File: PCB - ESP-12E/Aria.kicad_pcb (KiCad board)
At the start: 4 copper layers, 80 x 27 mm, 90 parts, among them J1 B2B-PH-K-S(LF)(SN), J2 B3B-PH-K-S(LF)(SN), J3 20021121-00010C4LF, J4 0475890001-MicroUSBPort, P1 CONN_01X18, P2 CONN_01X18, Q1 DMG2307L-7, Q2 DMG2307L-7, SW1 B3U-1000P, SW2 B3U-1000P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

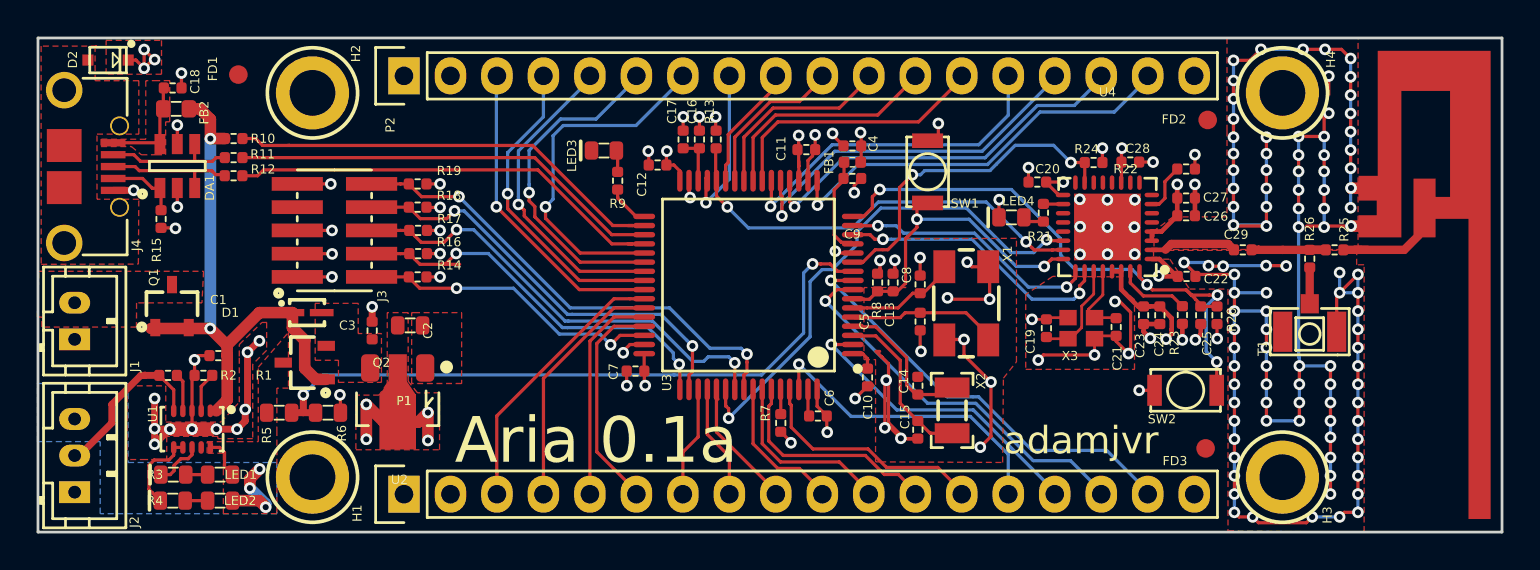
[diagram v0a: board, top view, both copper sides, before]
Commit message: ESP Footprint Error and RF improvement
ESP8285 footprint was wrong, made when I was still learning kiCAD.
Footprint change and entire topology reconstructed and rerouted. Added
ground pours and heavy via stitching to improve RF performance. Also
started an ESP-12E module based variant. Both will be fabbed at the same
time.
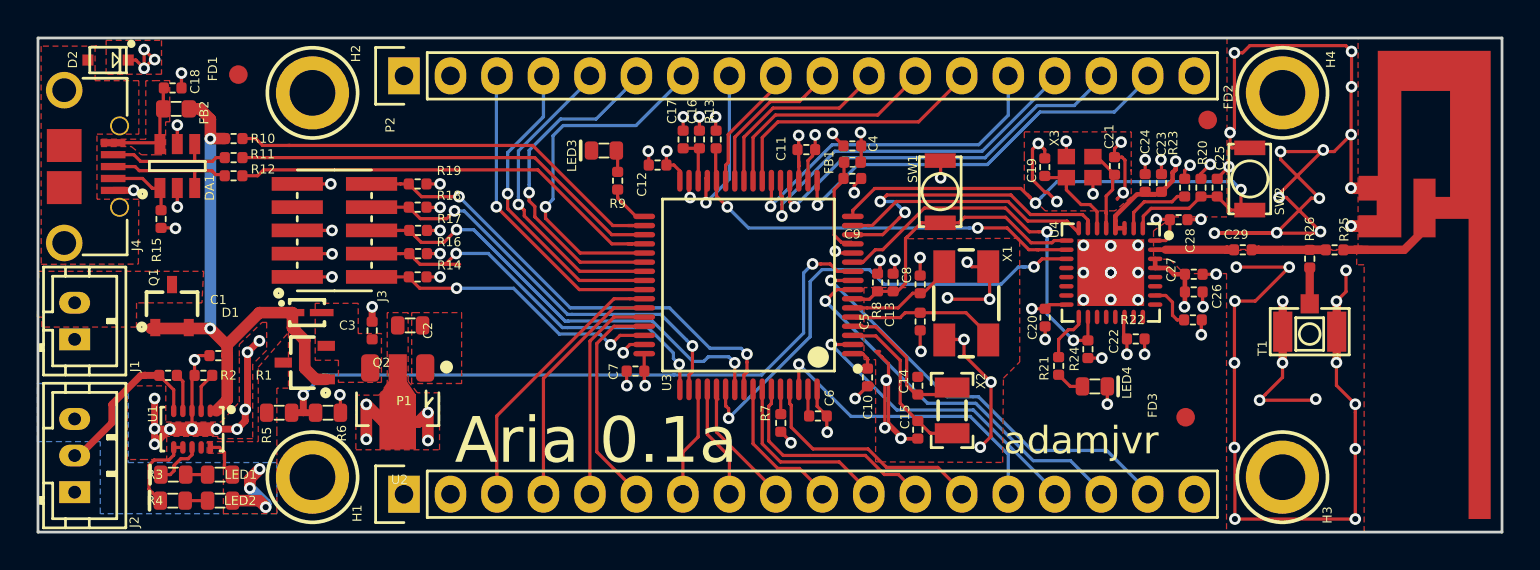
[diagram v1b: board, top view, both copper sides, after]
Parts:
- moved SW2 12.1 mm to (212.1, 79.3), turned to 270 degrees
- moved LED4 10.3 mm to (203.6, 90.6), turned to 0 degrees
- moved R24 10.2 mm to (203.2, 88.6), turned to 90 degrees
- moved C19 8.80 mm to (200.9, 78.6)
- moved X3 8.80 mm to (202.8, 78.6)
- moved C21 8.80 mm to (204.7, 78.6), turned to 90 degrees
- moved R21 8.41 mm to (201.6, 89.5), turned to 90 degrees
- moved R22 8.25 mm to (209.0, 87.0)
- moved C20 7.42 mm to (200.9, 86.9), turned to 270 degrees
- moved C23 7.29 mm to (207.3, 79.5), turned to 90 degrees
- moved C24 7.27 mm to (206.4, 79.5), turned to 90 degrees
- moved C25 7.03 mm to (210.3, 79.8), turned to 90 degrees
- moved R20 7.03 mm to (209.4, 79.8), turned to 90 degrees
- moved R23 6.96 mm to (208.5, 79.8), turned to 270 degrees
- moved C22 4.40 mm to (205.9, 88.0)
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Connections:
- R21 pad 1: Net-(R21-Pad1) -> Net-(LED4-Pad1)
- R21 pad 2: Net-(LED4-Pad1) -> Net-(R21-Pad2)
- U4 pad 16: Net-(U4-Pad16) -> Net-(R21-Pad2)
- U4 pad 18: Net-(R21-Pad1) -> Net-(U4-Pad18)
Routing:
- net GND: track 241.3 -> 218.1 mm, vias 172 -> 105
- net /MCU_STM32F446RET6/ESP_URX: track 15.3 -> 18.1 mm
- net Net-(R21-Pad2): track 0.00 -> 2.81 mm
- net /MCU_STM32F446RET6/ESP_PGM_MODE: track 18.4 -> 21.0 mm
- net /MCU_STM32F446RET6/ESPTOST_BOOT0: track 28.2 -> 26.2 mm
- net /MCU_STM32F446RET6/ESP_ST_RST: track 17.1 -> 15.5 mm, vias 2 -> 0
- net Net-(R21-Pad1): track 1.08 -> 0.00 mm
- net /MCU_STM32F446RET6/STM_ESP_RST: track 32.6 -> 31.7 mm, vias 4 -> 2
- net /MCU_STM32F446RET6/ESPTOST_BOOT1: track 23.7 -> 22.8 mm
- net /MCU_STM32F446RET6/ESP_UTX: track 14.1 -> 13.7 mm, vias 2 -> 0
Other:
- net class Default: clearance 0.1524 -> 0.1778
- rule trace_clearance: 0.1524 -> 0.1778
- rule trace_min: 0.1524 -> 0.1778

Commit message: DRC Cleared and Pictures
DRC cleared of errors for both Aria board designs. New pictures have
been added. Readme has also been updated.
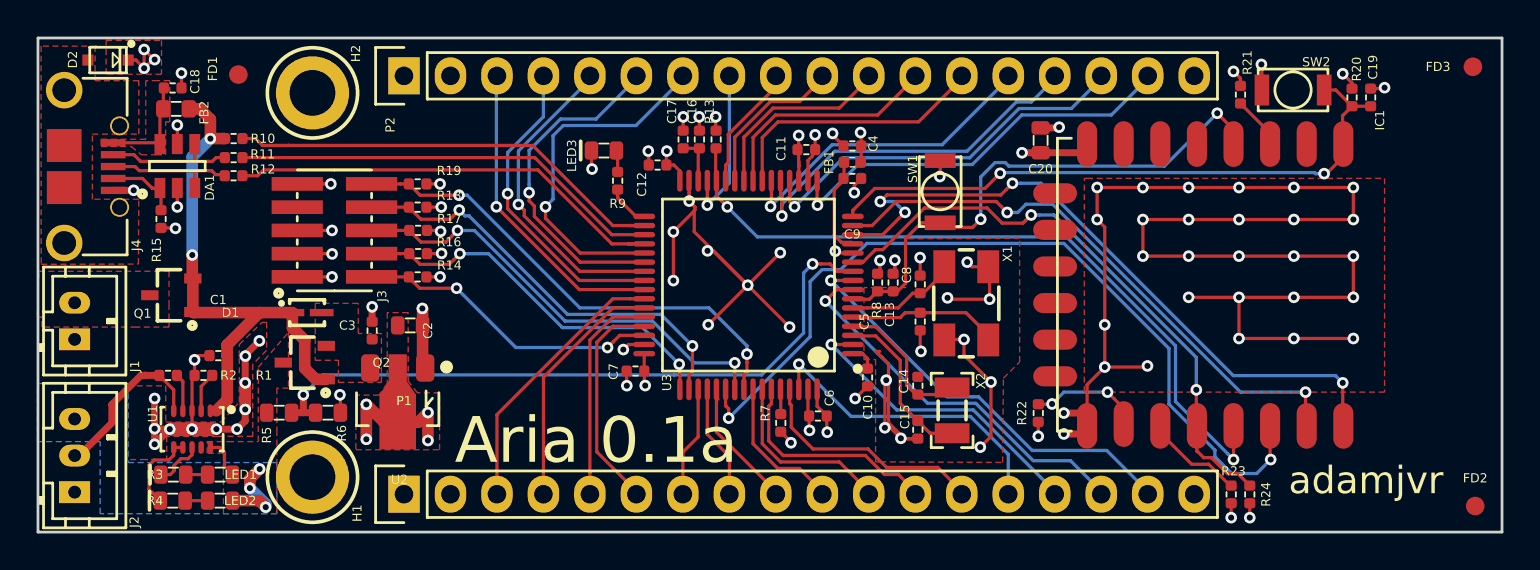
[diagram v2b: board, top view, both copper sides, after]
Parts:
- removed ANT1: Inverted_F_PCB_Antenna, PCB_Footprints:PCB_IF_ANT_2.4G
- removed C21: CL05C090CB5NNNC, PCB_Footprints:C0402
- removed C22, C23, C24, C25, C26, C27, C28: CL05B104JP5NNNC, PCB_Footprints:C0402
- removed C29: 600L5R6BT200T, PCB_Footprints:C0402
- removed H3, H4: M2.5_Hole, PCB_Footprints:M2.5_HOLE
- removed LED4: LTST-C193TBKT-5A, PCB_Footprints:LED0603
- removed R25, R26: ERJ-2GE0R00X, PCB_Footprints:R0402
- removed T1: 1909763-1, PCB_Footprints:1909763-1
- removed U4: ESP8285, PCB_Footprints:ESP8285
- removed X3: FA-128_26.0000MF10Z-AC3, PCB_Footprints:FA-128_26.0000MF10Z-AC3
- added IC1: ESP_12E, PCB_Footprints:ESP-12E, F.Cu at (217.2, 78.1)
- C19: value CL05C090CB5NNNC -> CL05B104JP5NNNC
- C20: value CL05B104JP5NNNC -> CL10A106KQ8NNNC; footprint PCB_Footprints:C0402 -> PCB_Footprints:C0603
- R21: value RC1005F102CS -> RC1005F103CS
- R22, R23: value RC1005F123CS -> RC1005F103CS
- moved FD2 25.7 mm to (224.4, 97.2)
- moved FD3 24.8 mm to (224.3, 73.2)
- moved C19 18.2 mm to (218.7, 74.8)
- moved R21 17.8 mm to (211.6, 74.7), turned to 270 degrees
- moved R23 17.0 mm to (211.1, 96.5), turned to 90 degrees
- moved R24 11.9 mm to (212.1, 96.5)
- moved R22 9.87 mm to (200.5, 92.1), turned to 270 degrees
- moved C20 9.69 mm to (200.7, 77.2), turned to 90 degrees
- moved R20 9.61 mm to (217.7, 74.8), turned to 270 degrees
- moved SW2 5.41 mm to (214.5, 74.4), turned to 0 degrees
- moved Q1 0.59 mm to (153.2, 85.6), turned to 180 degrees
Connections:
- C19 pad 1: Net-(C19-Pad1) -> /MCU_STM32F446RET6/STM_ESP_RST
- R20 pad 1: /MCU_STM32F446RET6/STM_ESP_RST -> +3V3
- R20 pad 2: +3V3 -> /MCU_STM32F446RET6/STM_ESP_RST
- R21 pad 1: Net-(LED4-Pad1) -> +3V3
- R22 pad 2: +3V3 -> GND
- R23 pad 1: GND -> +3V3
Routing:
- net GND: track 218.1 -> 188.0 mm, vias 105 -> 93
- net /MCU_STM32F446RET6/ESPTOST_BOOT0: track 26.2 -> 47.1 mm
- net /MCU_STM32F446RET6/ESP_URX: track 18.1 -> 36.8 mm, vias 2 -> 4
- net /MCU_STM32F446RET6/ESPTOST_BOOT1: track 22.8 -> 40.9 mm
- net /MCU_STM32F446RET6/ESP_UTX: track 13.7 -> 31.3 mm, vias 0 -> 2
- net /MCU_STM32F446RET6/ESP_ST_RST: track 15.5 -> 29.9 mm, vias 0 -> 2
- net +3V3: track 46.8 -> 34.2 mm, vias 25 -> 22
- net /MCU_STM32F446RET6/ESP_PGM_MODE: track 21.0 -> 32.6 mm
- net Net-(C19-Pad1): track 5.78 -> 0.00 mm
- net Net-(C21-Pad1): track 5.34 -> 0.00 mm
- net /WiFi-ESP8285/ANTENNA: track 4.93 -> 0.00 mm
- net /MCU_STM32F446RET6/STM_ESP_RST: track 31.7 -> 36.1 mm
- net /WiFi-ESP8285/LNA: track 4.31 -> 0.00 mm
- net Net-(IC1-Pad16): track 2.55 -> 5.62 mm, vias 0 -> 2
- net Net-(IC1-Pad17): track 3.84 -> 6.15 mm
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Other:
- board text added: "Aria-12E 0.1a"
